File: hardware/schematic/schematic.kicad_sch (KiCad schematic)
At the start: 6 parts, among them SW1 SW_SPST, SW2 SW_Push, U1 ESP32-C3-DevKitM-1

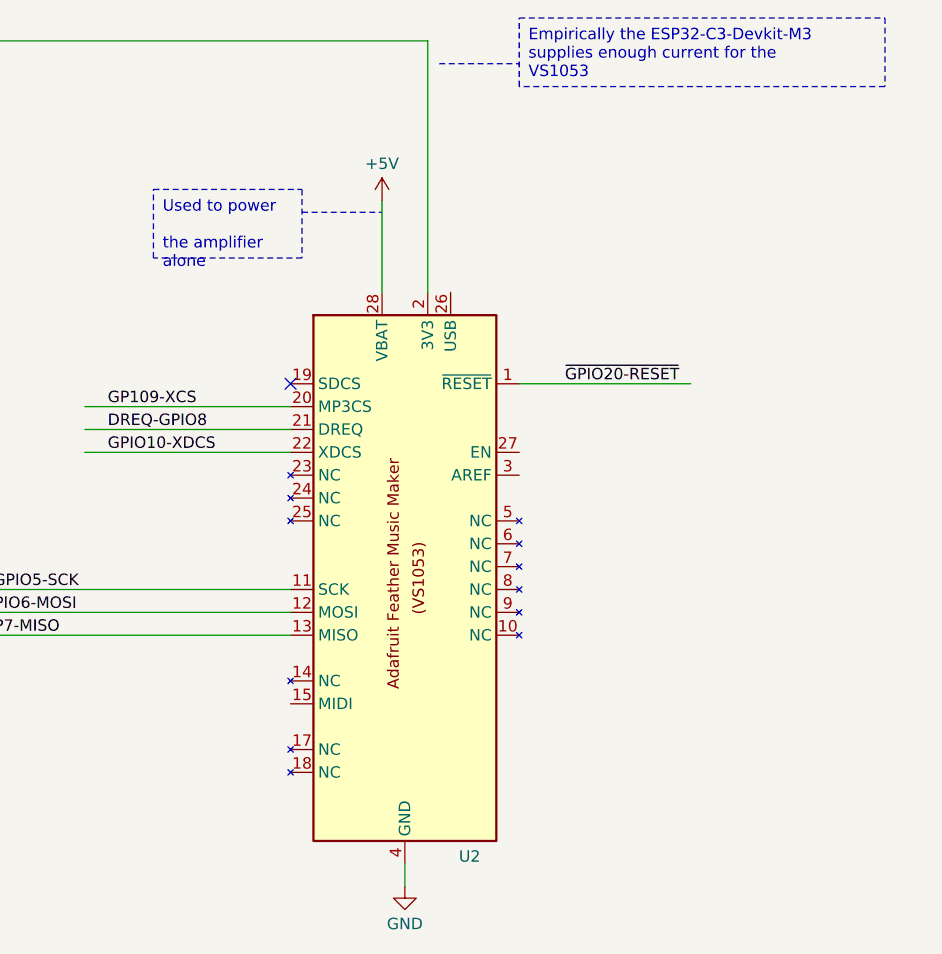
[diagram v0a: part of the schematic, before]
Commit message: Kicad migration to Linux
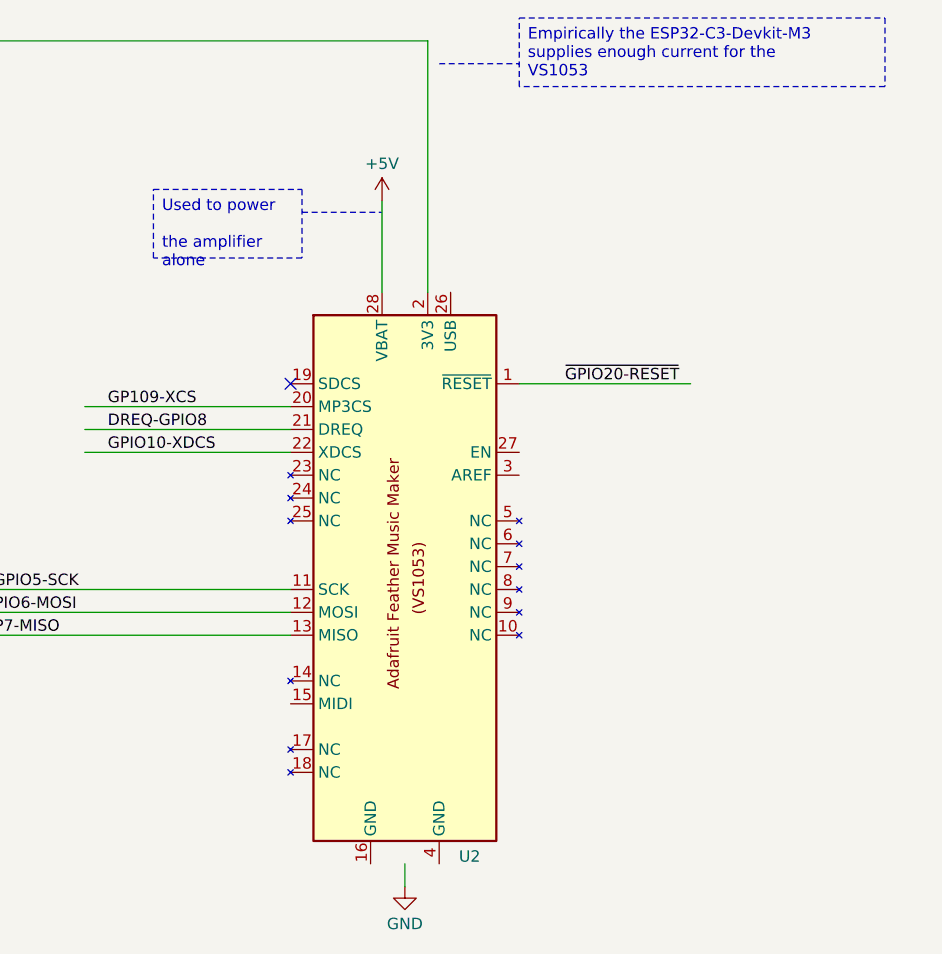
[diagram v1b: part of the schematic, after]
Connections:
- net GND: no longer U2.4 (GND)

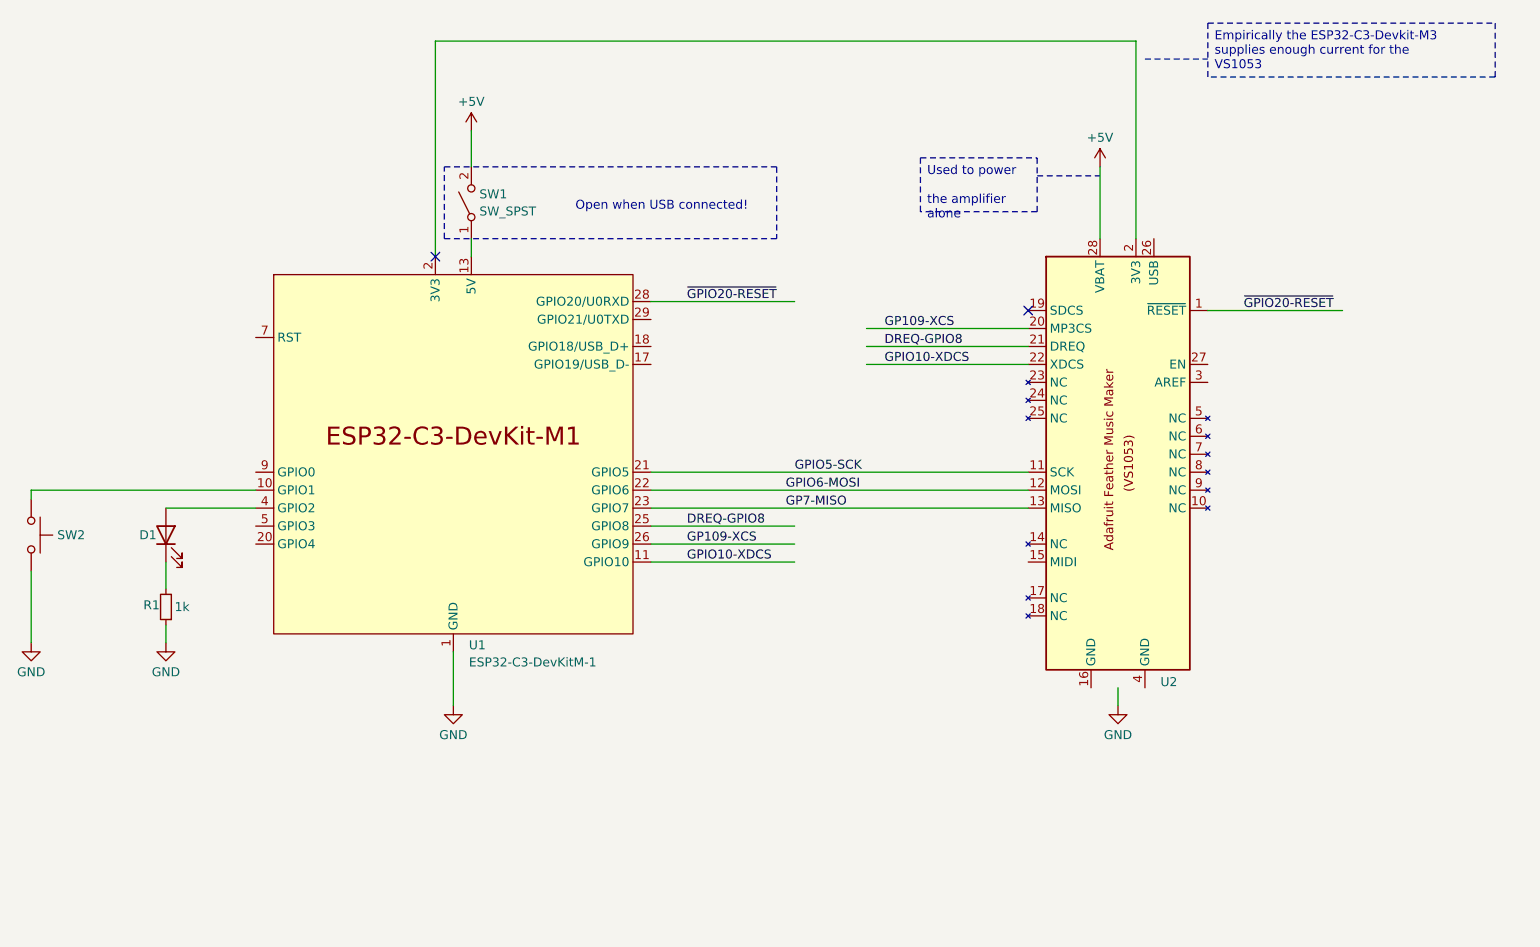
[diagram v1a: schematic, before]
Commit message: Powering of the VS1053
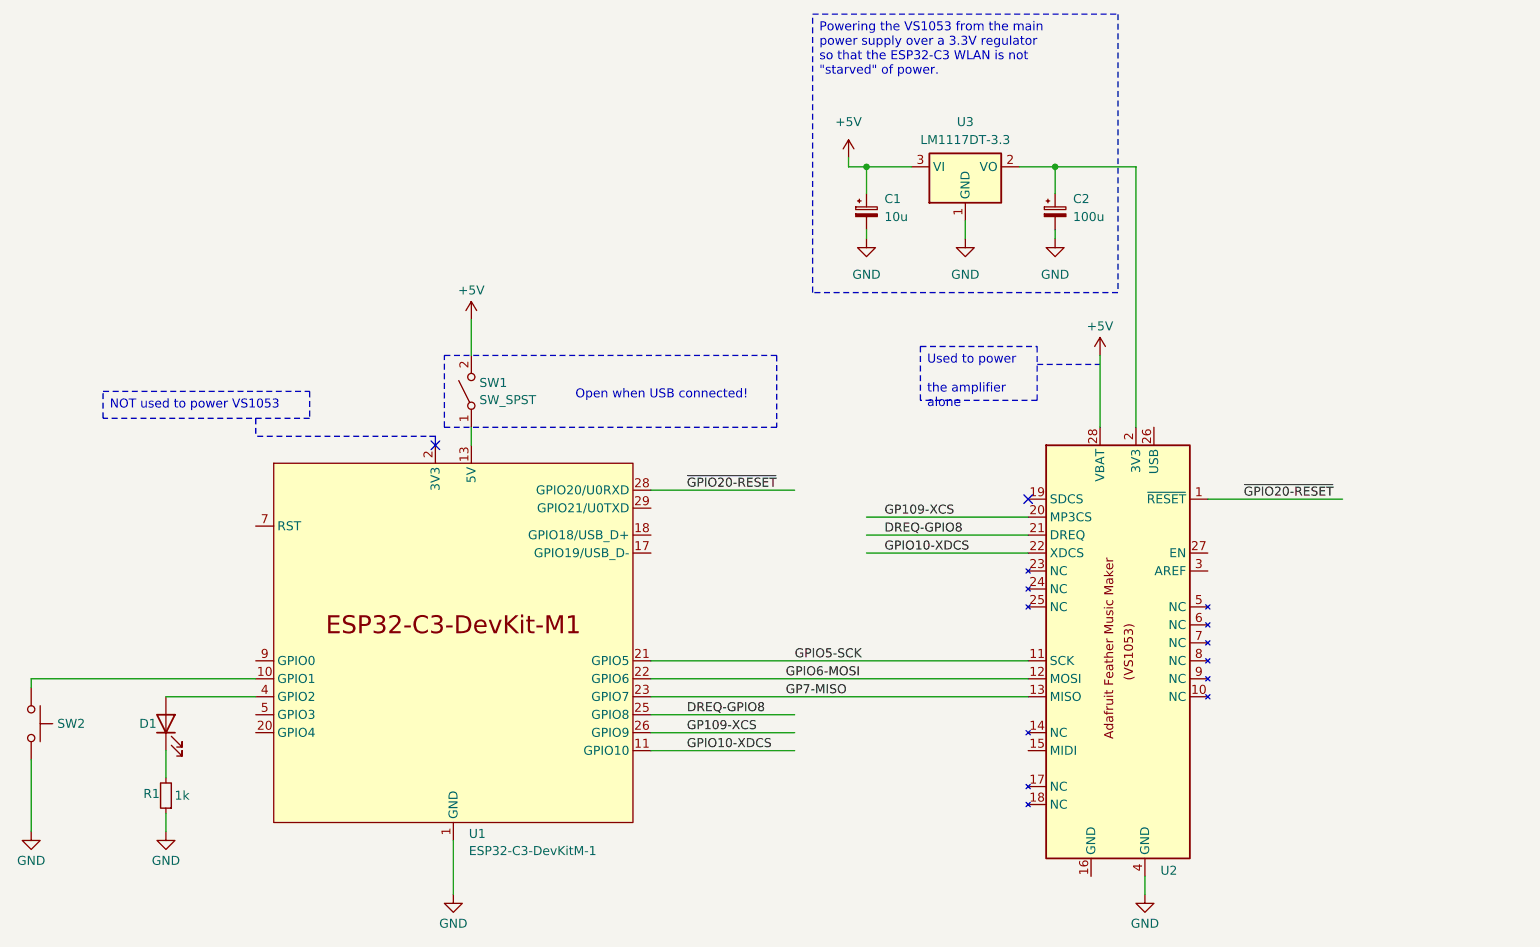
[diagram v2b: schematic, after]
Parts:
- added C1: 10u, symbol Device:C_Polarized_Small
- added C2: 100u, symbol Device:C_Polarized_Small
- added U3: LM1117DT-3.3, Package_TO_SOT_SMD:TO-252-3_TabPin2, symbol Regulator_Linear:LM1117DT-3.3
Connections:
- net +5V: now also C1.1, U3.3 (VI)
- net 3V3: no longer U2.2 (3V3)
- net GND: now also U2.4 (GND), C1.2, C2.2, U3.1 (GND)
- new net: C2.1, U2.2 (3V3), U3.2 (VO)
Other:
- moved on the sheet: D1, R1, SW1, SW2, U1, U2
